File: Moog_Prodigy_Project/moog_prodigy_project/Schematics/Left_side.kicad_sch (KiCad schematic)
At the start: 61 parts, among them Q1 CA3046, Q15 BC549, Q2 CA3046, Q4 CA3046, Q6 BC549, SW1 Switch_4x4, SW4 Switch_4x4, U2A1 OPA134, U2B3 OPA134, U5 NE5532, U6 LT1011CN8, U7 AD8066ARM, U8 NE5532

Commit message: PCB priprema i fix gresaka
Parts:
- RV14: renamed from R14; footprint Resistor_THT:R_Axial_DIN0207_L6.3mm_D2.5mm_P7.62mm_Horizontal -> Potentiometer_THT:Potentiometer_Bourns_3339P_Vertical_HandSoldering
- RV3: renamed from R3; footprint Resistor_THT:R_Axial_DIN0207_L6.3mm_D2.5mm_P7.62mm_Horizontal -> Potentiometer_THT:Potentiometer_Runtron_RM-065_Vertical
- RV42: renamed from R42; footprint Resistor_THT:R_Axial_DIN0207_L6.3mm_D2.5mm_P7.62mm_Horizontal -> Potentiometer_THT:Potentiometer_Bourns_3339P_Vertical_HandSoldering
- RV54: renamed from R54; footprint Resistor_THT:R_Axial_DIN0207_L6.3mm_D2.5mm_P7.62mm_Horizontal -> Potentiometer_THT:Potentiometer_Bourns_3339P_Vertical_HandSoldering
- RV7: renamed from R7; footprint Resistor_THT:R_Axial_DIN0207_L6.3mm_D2.5mm_P7.62mm_Horizontal -> Potentiometer_THT:Potentiometer_Runtron_RM-065_Vertical
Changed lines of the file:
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@@
 		(on_board yes)
 		(dnp no)
-		(property "Reference" "R3"
+		(property "Reference" "RV3"
 			(at 20.32 57.658 0)
 			(effects
@@
 			)
 		)
-		(property "Footprint" "Resistor_THT:R_Axial_DIN0207_L6.3mm_D2.5mm_P7.62mm_Horizontal"
+		(property "Footprint" "Potentiometer_THT:Potentiometer_Runtron_RM-065_Vertical"
 			(at 22.86 58.42 0)
 			(effects
@@
 			(project "moog_prodigy_project"
 				(path "/db469bdb-b6c3-4a16-9199-d4e6b8d556e8/6ca03b6b-5ad1-455d-b55d-f800979e8812"
-					(reference "R3")
+					(reference "RV3")
 					(unit 1)
 				)
@@
 		(on_board yes)
 		(dnp no)
-		(property "Reference" "R7"
+		(property "Reference" "RV7"
 			(at 81.28 54.356 90)
 			(effects
@@
 			)
 		)
-		(property "Footprint" "Resistor_THT:R_Axial_DIN0207_L6.3mm_D2.5mm_P7.62mm_Horizontal"
+		(property "Footprint" "Potentiometer_THT:Potentiometer_Runtron_RM-065_Vertical"
 			(at 81.28 58.42 0)
 			(effects
@@
 			(project "moog_prodigy_project"
 				(path "/db469bdb-b6c3-4a16-9199-d4e6b8d556e8/6ca03b6b-5ad1-455d-b55d-f800979e8812"
-					(reference "R7")
+					(reference "RV7")
 					(unit 1)
 				)
@@
 	)
 	(symbol
+		(lib_name "+12V_4")
+		(lib_id "power:+12V")
+		(at 22.86 50.8 0)
+		(unit 1)
+		(exclude_from_sim no)
+		(in_bom yes)
+		(on_board yes)
+		(dnp no)
+		(property "Reference" "#PWR045"
+			(at 22.86 54.61 0)
+			(effects
+				(font
+					(size 1.27 1.27)
+				)
+				(hide yes)
+			)
+		)
+		(property "Value" "+12V"
+			(at 22.86 46.99 0)
+			(effects
+				(font
+					(size 1.27 1.27)
+				)
+			)
+		)
+		(property "Footprint" ""
+			(at 22.86 50.8 0)
+			(effects
+				(font
+					(size 1.27 1.27)
+				)
+				(hide yes)
+			)
+		)
+		(property "Datasheet" ""
+			(at 22.86 50.8 0)
+			(effects
+				(font
+					(size 1.27 1.27)
+				)
+				(hide yes)
+			)
+		)
+		(property "Description" ""
+			(at 22.86 50.8 0)
+			(effects
+				(font
+					(size 1.27 1.27)
+				)
+			)
+		)
+		(pin "1"
+		)
+		(instances
+			(project "moog_prodigy_project"
+				(path "/db469bdb-b6c3-4a16-9199-d4e6b8d556e8/6ca03b6b-5ad1-455d-b55d-f800979e8812"
+					(reference "#PWR045")
+					(unit 1)
+				)
+			)
+		)
+	)
+	(symbol
 		(lib_id "minus12:-12V")
 		(at 191.77 106.68 180)
@@
 		(on_board yes)
 		(dnp no)
-		(property "Reference" "R54"
+		(property "Reference" "RV54"
 			(at 259.334 47.244 0)
 			(effects
@@
 			)
 		)
-		(property "Footprint" "Resistor_THT:R_Axial_DIN0207_L6.3mm_D2.5mm_P7.62mm_Horizontal"
+		(property "Footprint" "Potentiometer_THT:Potentiometer_Bourns_3339P_Vertical_HandSoldering"
 			(at 262.89 48.26 0)
 			(effects
@@
 			(project "moog_prodigy_project"
 				(path "/db469bdb-b6c3-4a16-9199-d4e6b8d556e8/6ca03b6b-5ad1-455d-b55d-f800979e8812"
-					(reference "R54")
+					(reference "RV54")
 					(unit 1)
 				)
@@
 	)
 	(symbol
-		(lib_id "power:+12V")
-		(at 22.86 50.8 0)
-		(unit 1)
-		(exclude_from_sim no)
-		(in_bom yes)
-		(on_board yes)
-		(dnp no)
-		(property "Reference" "#PWR045"
-			(at 22.86 54.61 0)
-			(effects
-				(font
-					(size 1.27 1.27)
-				)
-				(hide yes)
-			)
-		)
-		(property "Value" "+12V"
-			(at 22.86 46.99 0)
-			(effects
-				(font
-					(size 1.27 1.27)
-				)
-			)
-		)
-		(property "Footprint" ""
-			(at 22.86 50.8 0)
-			(effects
-				(font
-					(size 1.27 1.27)
-				)
-				(hide yes)
-			)
-		)
-		(property "Datasheet" ""
-			(at 22.86 50.8 0)
-			(effects
-				(font
-					(size 1.27 1.27)
-				)
-				(hide yes)
-			)
-		)
-		(property "Description" ""
-			(at 22.86 50.8 0)
-			(effects
-				(font
-					(size 1.27 1.27)
-				)
-			)
-		)
-		(pin "1"
-		)
-		(instances
-			(project "moog_prodigy_project"
-				(path "/db469bdb-b6c3-4a16-9199-d4e6b8d556e8/6ca03b6b-5ad1-455d-b55d-f800979e8812"
-					(reference "#PWR045")
-					(unit 1)
-				)
-			)
-		)
-	)
-	(symbol
 		(lib_id "Device:R")
 		(at 39.37 132.08 0)
@@
 		(on_board yes)
 		(dnp no)
-		(property "Reference" "R14"
+		(property "Reference" "RV14"
 			(at 37.592 138.684 0)
 			(effects
@@
 			)
 		)
-		(property "Footprint" "Resistor_THT:R_Axial_DIN0207_L6.3mm_D2.5mm_P7.62mm_Horizontal"
+		(property "Footprint" "Potentiometer_THT:Potentiometer_Bourns_3339P_Vertical_HandSoldering"
 			(at 39.37 139.7 0)
 			(effects
@@
 			(project "moog_prodigy_project"
 				(path "/db469bdb-b6c3-4a16-9199-d4e6b8d556e8/6ca03b6b-5ad1-455d-b55d-f800979e8812"
-					(reference "R14")
+					(reference "RV14")
 					(unit 1)
 				)
@@
 		(on_board yes)
 		(dnp no)
-		(property "Reference" "R42"
+		(property "Reference" "RV42"
 			(at 169.672 70.104 0)
 			(effects
@@
 			)
 		)
-		(property "Footprint" "Resistor_THT:R_Axial_DIN0207_L6.3mm_D2.5mm_P7.62mm_Horizontal"
+		(property "Footprint" "Potentiometer_THT:Potentiometer_Bourns_3339P_Vertical_HandSoldering"
 			(at 173.99 71.12 0)
 			(effects
@@
 			(project "moog_prodigy_project"
 				(path "/db469bdb-b6c3-4a16-9199-d4e6b8d556e8/6ca03b6b-5ad1-455d-b55d-f800979e8812"
-					(reference "R42")
+					(reference "RV42")
 					(unit 1)
 				)
@@
 	)
 	(symbol
-		(lib_id "power:GND")
-		(at 39.37 152.4 0)
-		(unit 1)
-		(exclude_from_sim no)
-		(in_bom yes)
-		(on_board yes)
-		(dnp no)
-		(fields_autoplaced yes)
-		(property "Reference" "#PWR01"
-			(at 39.37 158.75 0)
-			(effects
-				(font
-					(size 1.27 1.27)
-				)
-				(hide yes)
-			)
-		)
-		(property "Value" "GND"
-			(at 39.37 157.48 0)
-			(effects
-				(font
-					(size 1.27 1.27)
-				)
-			)
-		)
-		(property "Footprint" ""
-			(at 39.37 152.4 0)
-			(effects
-				(font
-					(size 1.27 1.27)
-				)
-				(hide yes)
-			)
-		)
-		(property "Datasheet" ""
-			(at 39.37 152.4 0)
-			(effects
-				(font
-					(size 1.27 1.27)
-				)
-				(hide yes)
-			)
-		)
-		(property "Description" "Power symbol creates a global label with name \"GND\" , ground"
-			(at 39.37 152.4 0)
-			(effects
-				(font
-					(size 1.27 1.27)
-				)
-				(hide yes)
-			)
-		)
-		(pin "1"
-		)
-		(instances
-			(project "moog_prodigy_project"
-				(path "/db469bdb-b6c3-4a16-9199-d4e6b8d556e8/6ca03b6b-5ad1-455d-b55d-f800979e8812"
-					(reference "#PWR01")
-					(unit 1)
-				)
-			)
-		)
-	)
-	(symbol
 		(lib_id "Device:C")
 		(at 77.47 105.41 180)
@@
 				)
 			)
+		)
+	)
+	(symbol
+		(lib_id "power:GND1")
+		(at 39.37 152.4 0)
+		(unit 1)
+		(exclude_from_sim no)
+		(in_bom yes)
+		(on_board yes)
+		(dnp no)
+		(fields_autoplaced yes)
+		(property "Reference" "#PWR0178"
+			(at 39.37 158.75 0)
+			(effects
+				(font
+					(size 1.27 1.27)
+				)
+				(hide yes)
+			)
+		)
+		(property "Value" "GND"
+			(at 39.37 157.48 0)
+			(effects
+				(font
+					(size 1.27 1.27)
+				)
+			)
+		)
+		(property "Footprint" ""
+			(at 39.37 152.4 0)
+			(effects
+				(font
+					(size 1.27 1.27)
+				)
+				(hide yes)
+			)
+		)
+		(property "Datasheet" ""
+			(at 39.37 152.4 0)
+			(effects
+				(font
+					(size 1.27 1.27)
+				)
+				(hide yes)
+			)
+		)
+		(property "Description" "Power symbol creates a global label with name \"GND1\" , ground"
+			(at 39.37 152.4 0)
+			(effects
+				(font
+					(size 1.27 1.27)
+				)
+				(hide yes)
+			)
+		)
+		(pin "1"
+		)
+		(instances
+			(project ""
+				(path "/db469bdb-b6c3-4a16-9199-d4e6b8d556e8/6ca03b6b-5ad1-455d-b55d-f800979e8812"
+					(reference "#PWR0178")
+					(unit 1)
+				)
+			)

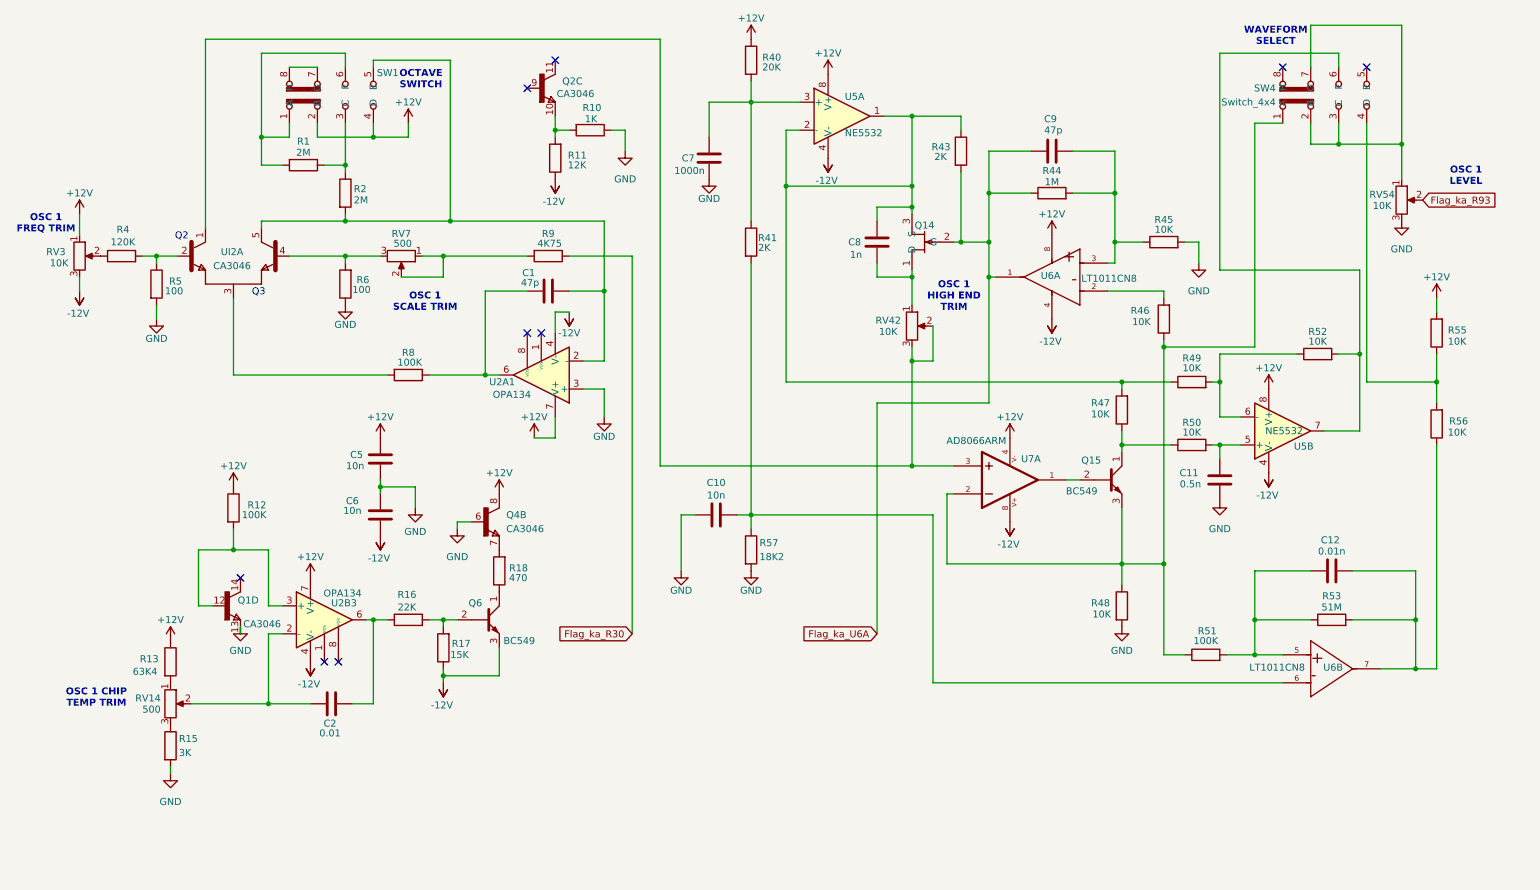
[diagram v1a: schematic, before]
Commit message: problemi sa ca3096, multiplicirani footprintovi
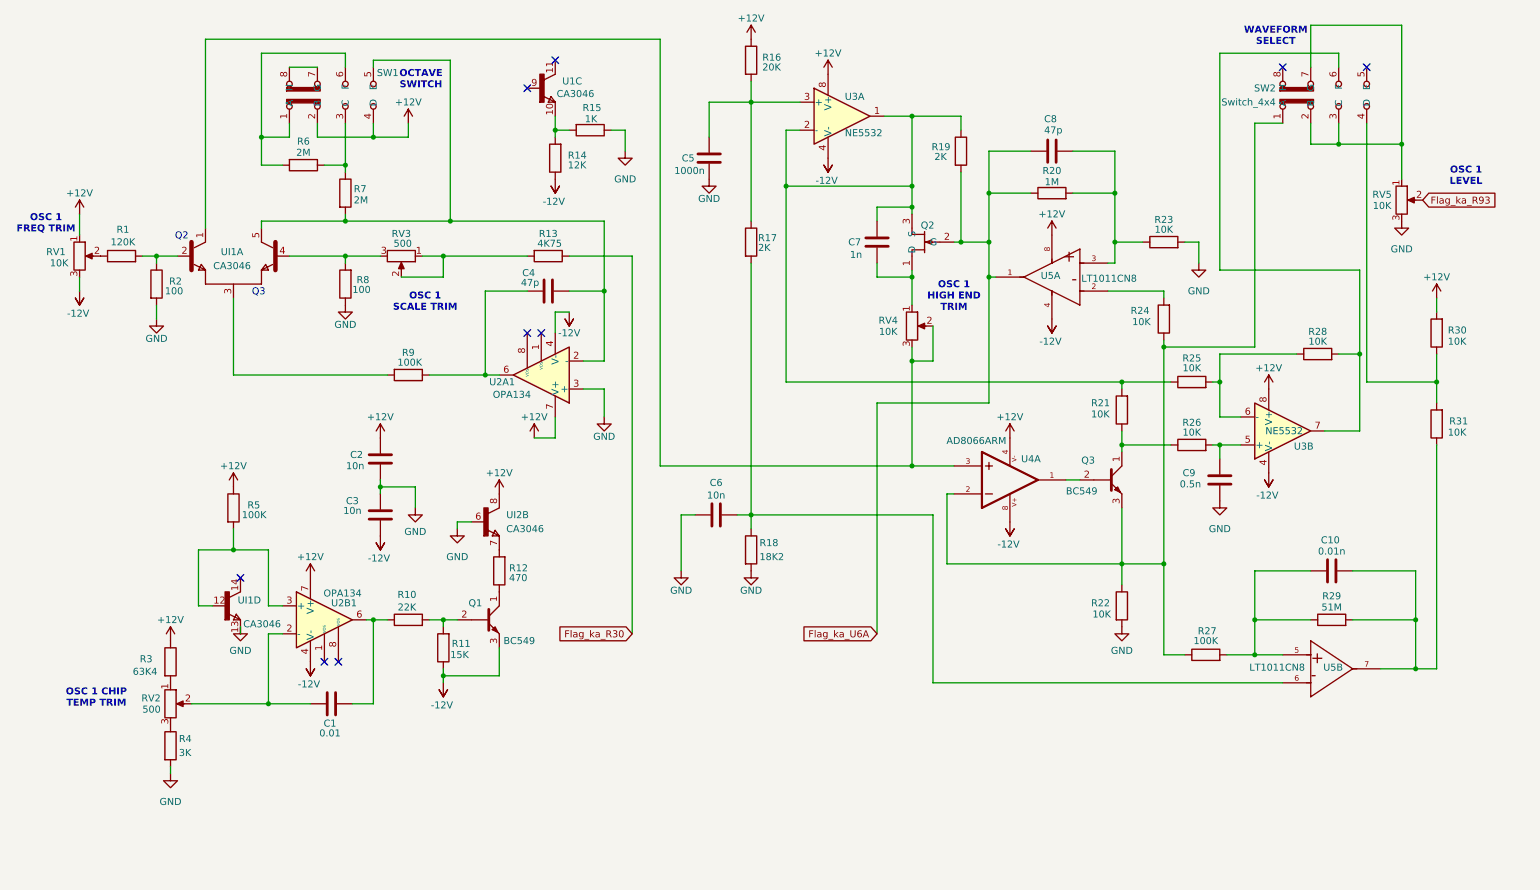
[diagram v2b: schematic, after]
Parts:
- renumbered C2 to C1, C12 to C10, C5 to C2, C6 to C3, C1 to C4, C7 to C5, C10 to C6, C8 to C7, C9 to C8, C11 to C9, Q6 to Q1, Q14 to Q2, Q15 to Q3, R4 to R1, R16 to R10, R17 to R11, R18 to R12, R9 to R13, R11 to R14, R10 to R15, R40 to R16, R41 to R17, R57 to R18, R43 to R19, R5 to R2, R44 to R20, R47 to R21, R48 to R22, R45 to R23, R46 to R24, R49 to R25, R50 to R26, R51 to R27, R52 to R28, R53 to R29, R13 to R3, R55 to R30, R56 to R31, R15 to R4, R12 to R5, R1 to R6, R2 to R7, R6 to R8, R8 to R9, RV3 to RV1, RV14 to RV2, RV7 to RV3, RV42 to RV4, RV54 to RV5, SW4 to SW2, Q2 to U1, U8 to U2, U2B3 to U2B1, U5 to U3, U7 to U4, U6 to U5, Q1 to UI1, UI2 to UI1, Q4 to UI2

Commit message: CA3046 leva strana seme update
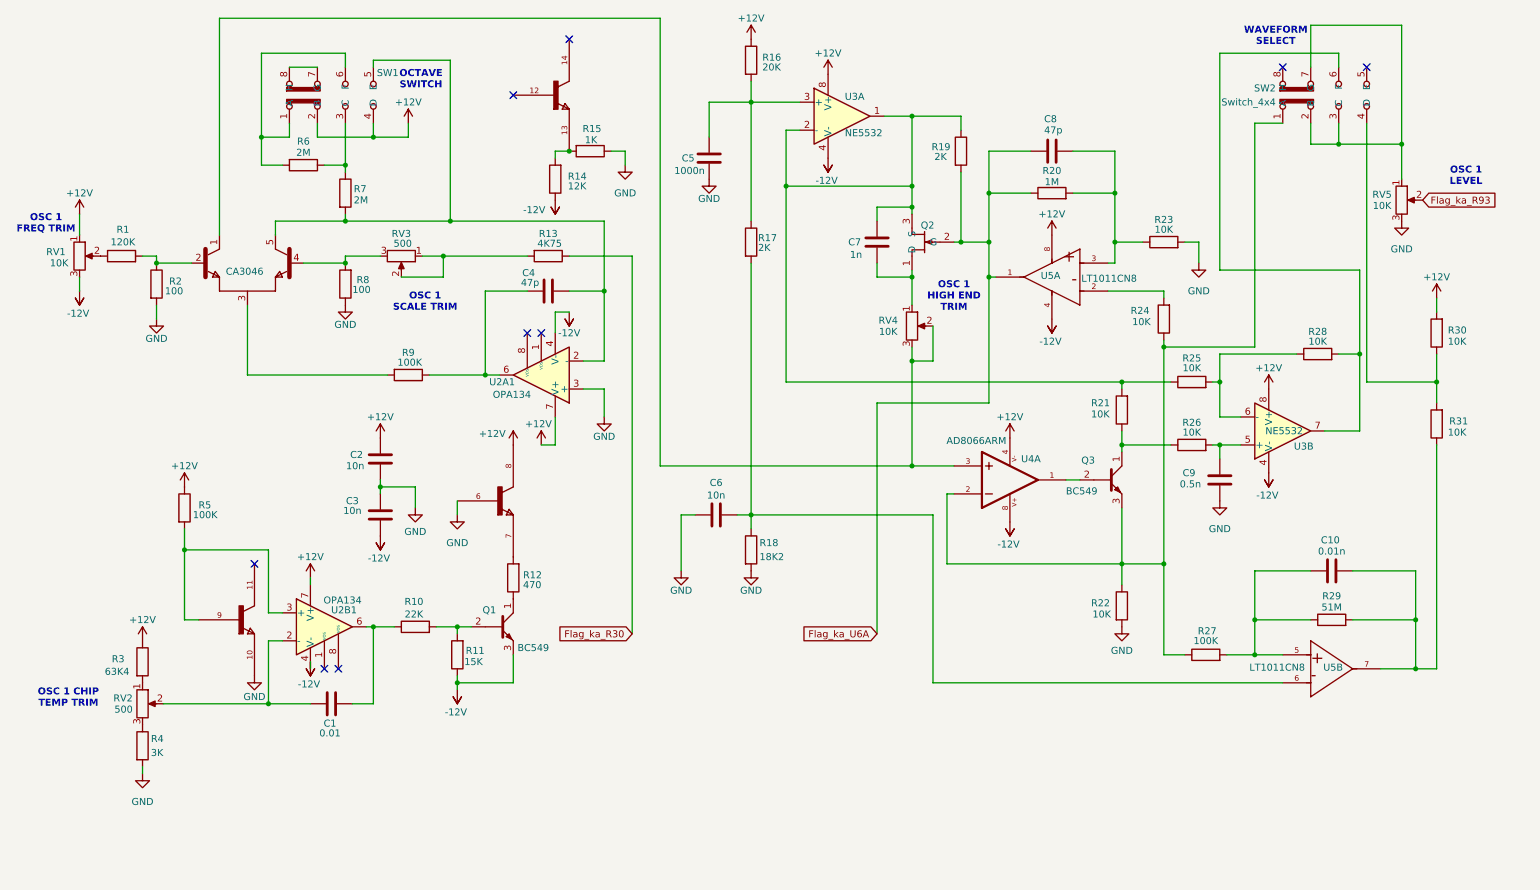
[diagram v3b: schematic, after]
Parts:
- removed U1, UI1, UI2: CA3046, CA3046:DIL14, symbol CA3046:CA3046
- added CA3046: CA3046, CA3046:DIL14, symbol CA3046:CA3046_novi_2
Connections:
- net +12V: now also CA3046.8
- net GND: now also CA3046.10, CA3046.6
- net at R8.2, RV3.3: now also CA3046.4
- net at R1.2, R2.1: now also CA3046.2
- net at C4.2, R7.2, SW1.5 (E)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: now also CA3046.5
- net at R12.2: now also CA3046.7
- net at R14.2, R15.2: now also CA3046.13
- net at R9.2: now also CA3046.3
- net at RV4.2, RV4.3, U4.3: now also CA3046.1
- net at R5.2, U2B1.3 (+): now also CA3046.9
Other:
- note removed: "Q2"
- note removed: "Q3"
- moved on the sheet: Q1, R10, R11, R12, R14, R15, R3, R4, R5, RV2, U2B1

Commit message: Left side PCB update final
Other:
- moved on the sheet: C1, C10, C2, C3, C4, C5, C6, C7, C8, C9, CA3046, Q1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

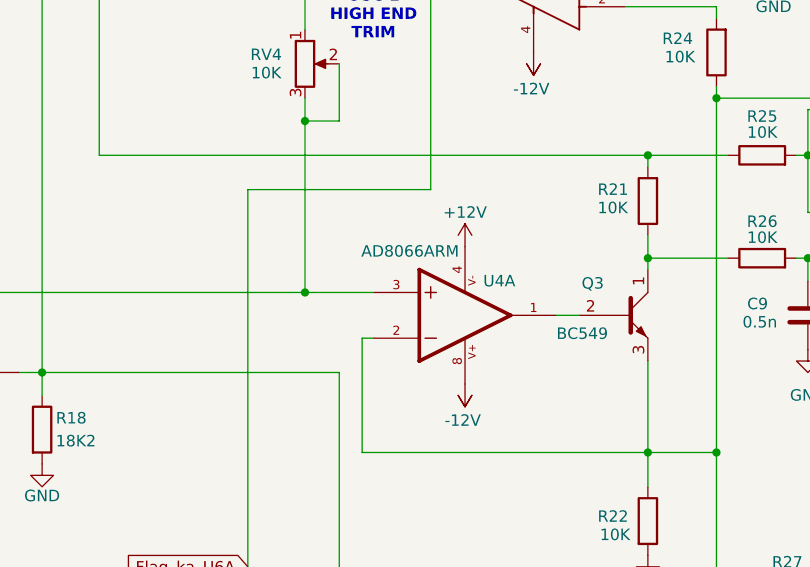
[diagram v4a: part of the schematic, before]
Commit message: SMD component to THT component update PCB
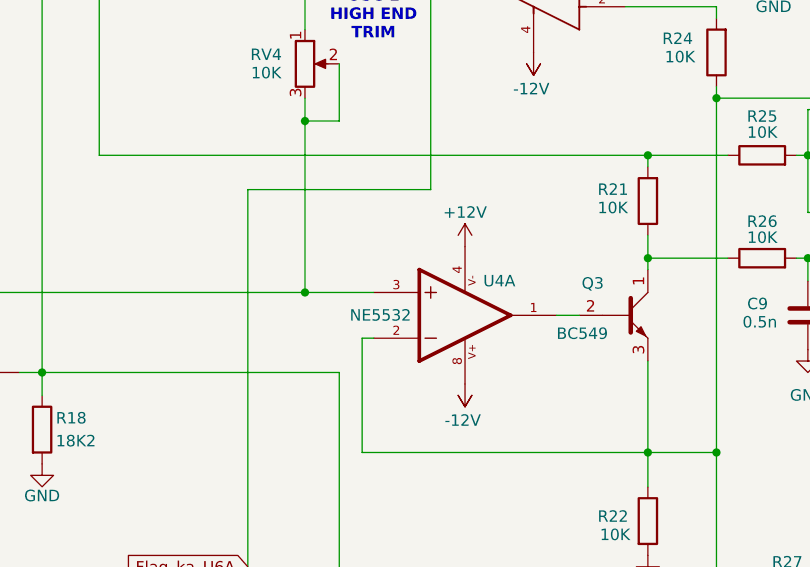
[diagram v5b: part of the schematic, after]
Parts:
- U4: value AD8066ARM -> NE5532; footprint AD8066ARM:SOP65P490X110-8N -> NE5532AP:DIP794W45P254L1016H508Q8
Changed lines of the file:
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@@
 			)
 		)
-		(property "Value" "AD8066ARM"
-			(at 188.214 104.648 0)
+		(property "Value" "NE5532"
+			(at 184.912 111.76 0)
 			(effects
 				(font
@@
 			)
 		)
-		(property "Footprint" "AD8066ARM:SOP65P490X110-8N"
+		(property "Footprint" "NE5532AP:DIP794W45P254L1016H508Q8"
 			(at 194.31 111.76 0)
 			(effects

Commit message: Routhed PCB final 17.05.2026
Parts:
- Q2: footprint BF256C:TO92127P478H483-3 -> Package_TO_SOT_THT:TO-92_Inline
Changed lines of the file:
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@@
 			)
 		)
-		(property "Footprint" "BF256C:TO92127P478H483-3"
+		(property "Footprint" "Package_TO_SOT_THT:TO-92_Inline"
 			(at 181.61 66.04 0)
 			(effects

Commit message: Fix 1 nakon review-a 27.05.2026
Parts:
- removed RV1: 10K, Potentiometer_THT:Potentiometer_Runtron_RM-065_Vertical, symbol Device:R_Potentiometer
- removed RV2: 500, Potentiometer_THT:Potentiometer_Bourns_3339P_Vertical_HandSoldering, symbol Device:R_Potentiometer
- removed RV3: 500, Potentiometer_THT:Potentiometer_Runtron_RM-065_Vertical, symbol Device:R_Potentiometer
- removed RV4: 10K, Potentiometer_THT:Potentiometer_Bourns_3339P_Vertical_HandSoldering, symbol Device:R_Potentiometer
- added RV1, RV4: 10K, Potentiometer_THT:Potentiometer_Bourns_3339P_Vertical_HandSoldering, symbol Device:R_Potentiometer_Trim
- added RV2, RV3: 500, Potentiometer_THT:Potentiometer_Bourns_3339P_Vertical_HandSoldering, symbol Device:R_Potentiometer_Trim
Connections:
- net +12V: now also CA3046., RV1.1; no longer CA3046.8
- net -12V: now also Q1. (E), RV1.3; no longer Q1.3 (E)
- net Flag_ka_U6A: now also Q2.; no longer Q2.2 (G)
- net GND: now also CA3046.; no longer CA3046.10, CA3046.6
- net at R1.1: now also RV1.2
- net at R22.1, R24.1, R27.1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: now also Q3. (E); no longer Q3.3 (E)
- net at R13.2: now also RV3.1, RV3.2
- net at R8.2: now also CA3046., RV3.3; no longer CA3046.4
- net at R1.2, R2.1: now also CA3046.; no longer CA3046.2
- net at C4.2, R7.2, SW1.5 (E)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: now also CA3046.; no longer CA3046.5
- net at R12.1: now also Q1. (E); no longer Q1.1 (C)
- net at R10.2, R11.2: now also Q1. (E); no longer Q1.2 (B)
- net at C7.2, R19.1, R21.2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: now also Q2.; no longer Q2.3 (S)
- net at R12.2: now also CA3046.; no longer CA3046.7
- net at C7.1: now also Q2., RV4.1; no longer Q2.1 (D)
- net at R3.2: now also RV2.1
- net at R9.2: now also CA3046.; no longer CA3046.3
- net at U4.1: now also Q3. (E); no longer Q3.2 (B)
- net at U4.3: now also CA3046., RV4.2, RV4.3; no longer CA3046.1
- net at R14.2, R15.2: now also CA3046.; no longer CA3046.13
- net at C1.1, U2B1.2 (-): now also RV2.2
- net at R5.2, U2B1.3 (+): now also CA3046.; no longer CA3046.9
- net at R21.1, R26.1: now also Q3. (E); no longer Q3.1 (C)
- net at R4.1: now also RV2.3
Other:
- title: (none) -> Prvi segment leve strane šeme

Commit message: Latest checkpoints update 05.06.2026
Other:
- note added: "Promena oktava po položaju preklopnika: 32' krajnji levi položaj 16' srednji položaj 8' krajnji desni položaj"
- note added: "Talasni oblik signala po promeni položaja preklopnika: Rampa - krajnji levi položaj Trougao - srednji položaj Četvrtke - krajnji desni položaj"
- moved on the sheet: C1, C10, C2, C3, C4, C5, C6, C7, C8, C9, CA3046, Q1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
